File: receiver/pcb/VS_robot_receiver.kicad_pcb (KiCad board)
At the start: 2 copper layers, 45 x 21 mm, 6 parts, among them J2 outputs

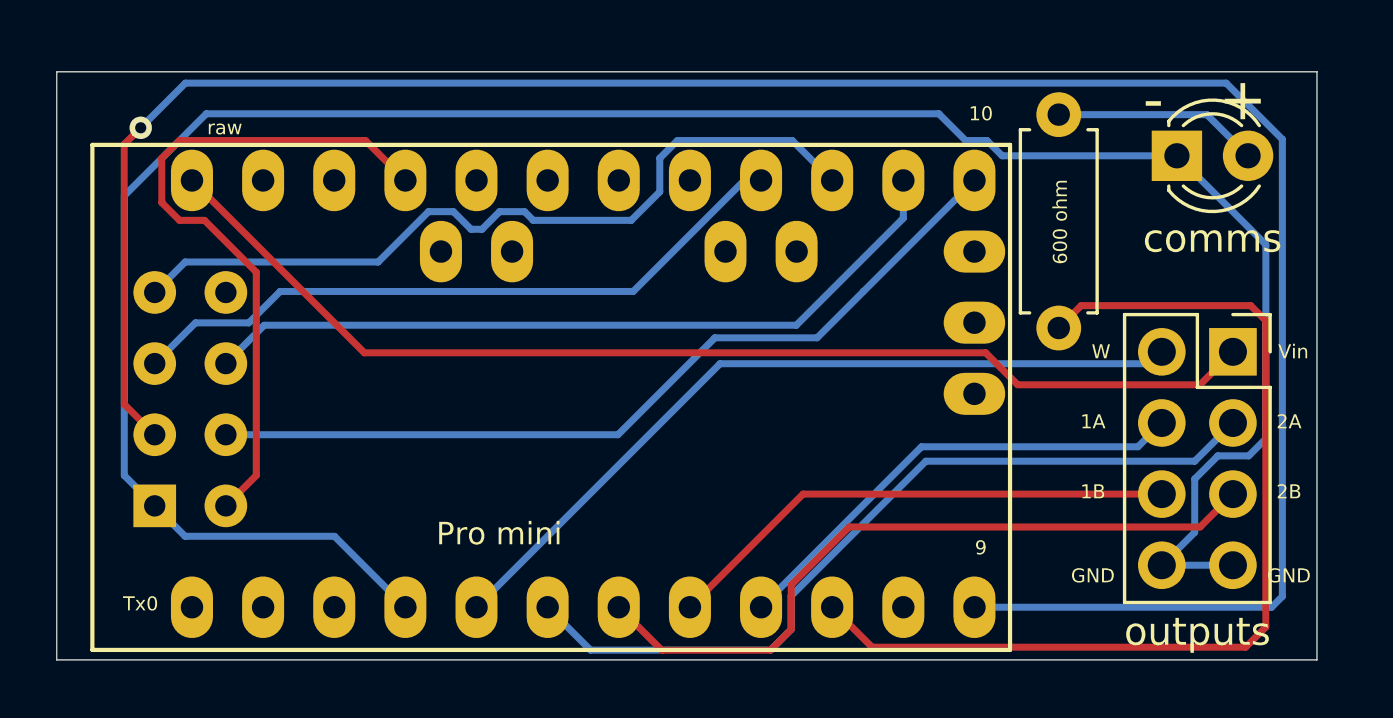
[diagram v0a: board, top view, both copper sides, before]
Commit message: V1.3 of Receiver and 1.2 of Transmitter. These versions were ordered 6/21/22
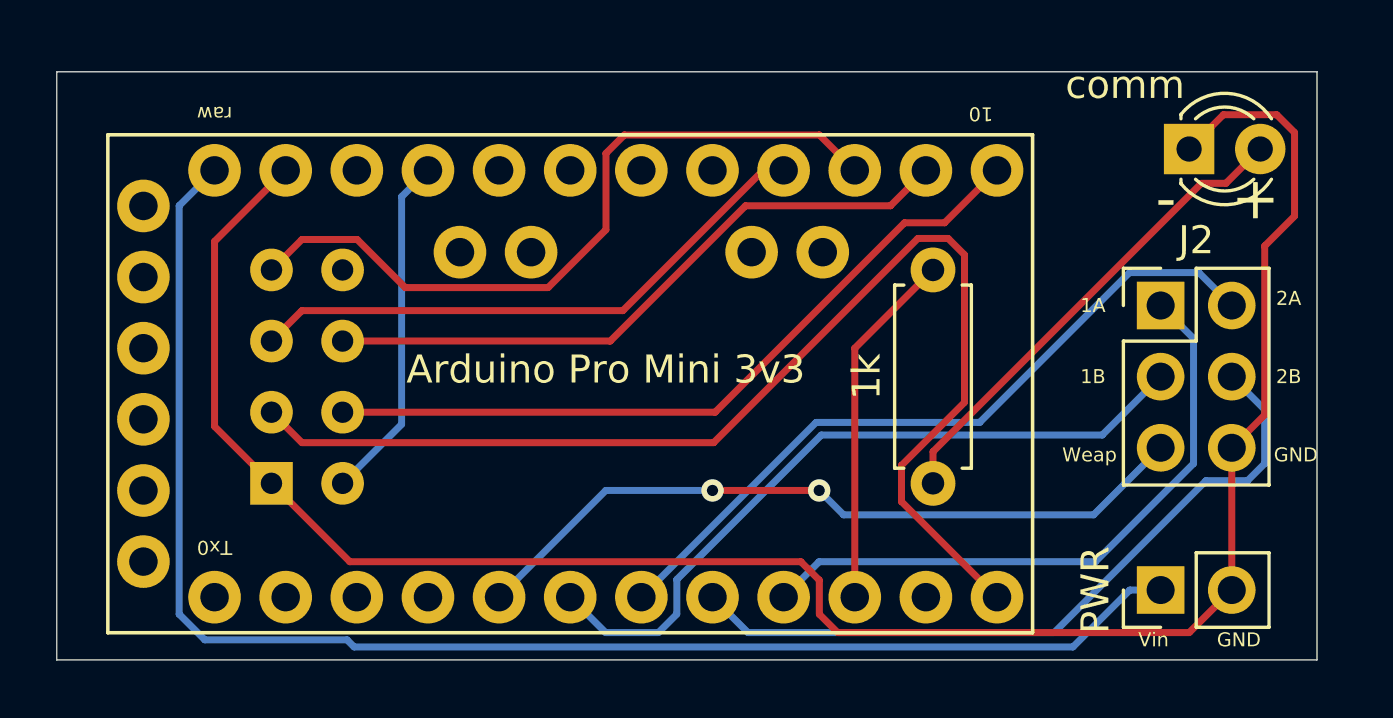
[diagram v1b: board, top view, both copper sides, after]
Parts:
- removed 600 ohm: 600, Resistor_THT:R_Axial_DIN0207_L6.3mm_D2.5mm_P7.62mm_Horizontal
- removed D1: comms, LED_THT:LED_D3.0mm
- removed G***: LOGO, vslogo:vslogo
- removed NRF24L01: NRF24L01_Breakout, RF_Module:nRF24L01_Breakout
- removed Pro mini: arduino-pro-mini, arduino-footprint:pro_mini
- added 1k: 680ohm, Resistor_THT:R_Axial_DIN0207_L6.3mm_D2.5mm_P7.62mm_Horizontal, F.Cu at (161.3, 107.7)
- added Arduino Pro Mini 3v3: ARDUINO_PRO_MINI, arduino:MODULE_ARDUINO_PRO_MINI, F.Cu at (148.3, 104.1)
- added NRF24: NRF24L01_Breakout, RF_Module:nRF24L01_Breakout, B.Cu at (137.7, 107.7)
- added PWR: Conn_01x02_Female, Connector_PinHeader_2.54mm:PinHeader_1x02_P2.54mm_Vertical, F.Cu at (169.4, 111.5)
- added comm: LED, LED_THT:LED_D3.0mm, F.Cu at (170.4, 95.8)
- J2: value outputs -> Conn_02x03_Odd_Even; footprint Connector_PinSocket_2.54mm:PinSocket_2x04_P2.54mm_Vertical -> Connector_PinHeader_2.54mm:PinHeader_2x03_P2.54mm_Vertical
- moved J2 3.07 mm to (169.4, 101.3)
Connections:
- J2 pad 1: +5V -> Net-(J2-Pad1)
- J2 pad 6: Net-(J2-Pad6) -> GND
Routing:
- net Net-(U1-Pad12): track 81.4 -> 0.00 mm, vias 1 -> 0
- net Net-(U1-Pad3): track 0.00 -> 43.0 mm
- net Net-(U1-Pad13): track 30.5 -> 0.00 mm
- net Net-(U1-Pad15): track 28.5 -> 0.00 mm
- net Net-(U1-Pad14): track 27.7 -> 0.00 mm
- net Net-(U1-Pad4): track 0.00 -> 26.9 mm
- net Net-(U1-Pad7): track 0.00 -> 26.4 mm
- net Net-(U1-Pad16): track 24.4 -> 0.00 mm
- net Net-(U1-Pad6): track 0.00 -> 23.4 mm
- net Net-(J2-Pad1): track 0.00 -> 22.7 mm
- net Net-(R1-Pad2): track 35.3 -> 12.8 mm
- net Net-(U1-Pad5): track 0.00 -> 20.8 mm
- net Net-(J2-Pad6): track 18.5 -> 0.00 mm
- net +5V: track 40.7 -> 52.7 mm
- net +3V3: track 24.3 -> 12.4 mm
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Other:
- board text added: "Combat Robot Receiver V1.3"
- board text added: "Weap"
- board text removed: "9"
- board text removed: "Combat Robot Receiver V1.2"
- board text removed: "W"

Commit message: tweaked wheel hub after test prints
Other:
- board text added: "Vector Space"
